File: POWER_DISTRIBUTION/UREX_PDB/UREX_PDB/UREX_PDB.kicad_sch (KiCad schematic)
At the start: 23 parts, among them IC1 TCAN1044VDDFR, IC5 TCA6408ARGTR, J12 S3B-PH-SM4-TB_LF__SN_, U1 ESP32-WROOM-32UE-R2

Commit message: fixed jarring pcb issues
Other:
- note added: "UARTS are flipped here issue:net is unused in actual board!"
- note removed: "UARTS are flipped here"
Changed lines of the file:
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@@
 		)
 	)
-	(text "UARTS are flipped here"
+	(text "UARTS are flipped here\nissue:net is unused in actual board!\n\n"
 		(exclude_from_sim no)
-		(at 113.792 71.628 0)
+		(at 121.92 71.12 0)
 		(effects
 			(font

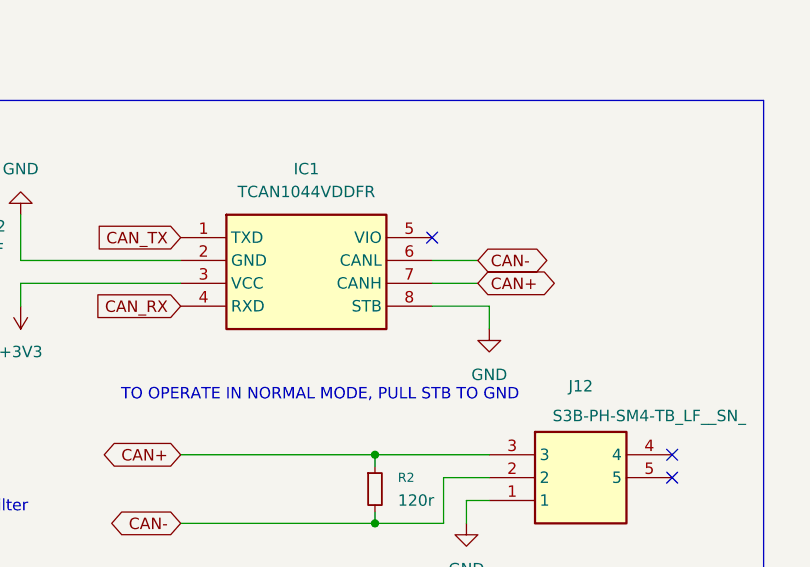
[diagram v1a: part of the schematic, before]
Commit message: changed CAN IC
TCAN1044 to TCAN332D, pin to pin compatible
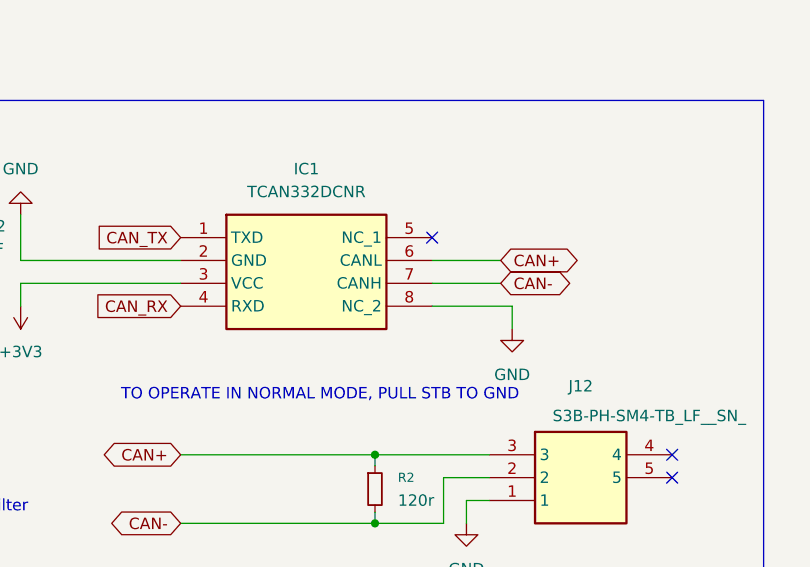
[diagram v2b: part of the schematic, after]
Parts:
- removed IC1: TCAN1044VDDFR, SamacSys_Parts:SOT65P280X110-8N, symbol SamacSys_COMMS:TCAN1044VDDFR
- added IC1: TCAN332DCNR, SOT65P280X145-8N, symbol SamacSys_Parts:TCAN332DCNR
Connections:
- net +3V3: now also IC1.3 (VCC)
- net CAN+: now also IC1.6 (CANL)
- net CAN-: now also IC1.7 (CANH)
- net CAN_RX: now also IC1.4 (RXD)
- net CAN_TX: now also IC1.1 (TXD)
- net GND: now also IC1.2 (GND), IC1.8 (NC_2)
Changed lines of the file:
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@@
 	(wire
 		(pts
-			(xy 33.02 44.45) (xy 44.45 44.45)
+			(xy 246.38 31.75) (xy 254 31.75)
 		)
 		(stroke
@@
 	(wire
 		(pts
-			(xy 240.03 60.96) (xy 247.65 60.96)
+			(xy 33.02 44.45) (xy 44.45 44.45)
 		)
 		(stroke
@@
 	(wire
 		(pts
-			(xy 252.73 36.83) (xy 252.73 39.37)
+			(xy 240.03 60.96) (xy 247.65 60.96)
 		)
 		(stroke
@@
 	(wire
 		(pts
-			(xy 246.38 31.75) (xy 251.46 31.75)
+			(xy 255.27 36.83) (xy 255.27 39.37)
 		)
 		(stroke
@@
 	(wire
 		(pts
-			(xy 246.38 36.83) (xy 252.73 36.83)
+			(xy 250.19 58.42) (xy 250.19 60.96)
 		)
 		(stroke
@@
 	(wire
 		(pts
-			(xy 250.19 58.42) (xy 250.19 60.96)
+			(xy 203.2 78.74) (xy 203.2 82.55)
 		)
 		(stroke
@@
 	(wire
 		(pts
-			(xy 203.2 78.74) (xy 203.2 82.55)
+			(xy 246.38 34.29) (xy 254 34.29)
 		)
 		(stroke
@@
 	(wire
 		(pts
-			(xy 246.38 34.29) (xy 251.46 34.29)
+			(xy 218.44 60.96) (xy 240.03 60.96)
 		)
 		(stroke
@@
 	(wire
 		(pts
-			(xy 218.44 60.96) (xy 240.03 60.96)
+			(xy 240.03 53.34) (xy 252.73 53.34)
 		)
 		(stroke
@@
 	(wire
 		(pts
-			(xy 240.03 53.34) (xy 252.73 53.34)
+			(xy 198.12 127) (xy 198.12 120.65)
 		)
 		(stroke
@@
 	(wire
 		(pts
-			(xy 198.12 127) (xy 198.12 120.65)
+			(xy 246.38 36.83) (xy 255.27 36.83)
 		)
 		(stroke
@@
 	(global_label "CAN-"
 		(shape bidirectional)
-		(at 251.46 31.75 0)
+		(at 254 34.29 0)
 		(fields_autoplaced yes)
 		(effects
@@
 		)
 		(property "Intersheetrefs" "${INTERSHEET_REFS}"
-			(at 260.818 31.75 0)
+			(at 263.358 34.29 0)
 			(hide yes)
 			(show_name no)
@@
 	(global_label "CAN+"
 		(shape bidirectional)
-		(at 251.46 34.29 0)
+		(at 254 31.75 0)
 		(fields_autoplaced yes)
 		(effects
@@
 		)
 		(property "Intersheetrefs" "${INTERSHEET_REFS}"
-			(at 260.818 34.29 0)
+			(at 263.358 31.75 0)
 			(hide yes)
 			(show_name no)
@@
 	)
 	(symbol
-		(lib_id "SamacSys_COMMS:TCAN1044VDDFR")
-		(at 218.44 29.21 0)
-		(unit 1)
-		(body_style 1)
-		(exclude_from_sim no)
-		(in_bom yes)
-		(on_board yes)
-		(in_pos_files yes)
-		(dnp no)
-		(fields_autoplaced yes)
-		(property "Reference" "IC1"
-			(at 232.41 21.59 0)
-			(show_name no)
-			(do_not_autoplace no)
-			(effects
-				(font
-					(size 1.27 1.27)
-				)
-			)
-		)
-		(property "Value" "TCAN1044VDDFR"
-			(at 232.41 24.13 0)
-			(show_name no)
-			(do_not_autoplace no)
-			(effects
-				(font
-					(size 1.27 1.27)
-				)
-			)
-		)
-		(property "Footprint" "SamacSys_Parts:SOT65P280X110-8N"
-			(at 242.57 124.13 0)
-			(hide yes)
-			(show_name no)
-			(do_not_autoplace no)
-			(effects
-				(font
-					(size 1.27 1.27)
-				)
-				(justify left top)
-			)
-		)
-		(property "Datasheet" "https://www.ti.com/lit/gpn/TCAN1044V"
-			(at 242.57 224.13 0)
-			(hide yes)
-			(show_name no)
-			(do_not_autoplace no)
-			(effects
-				(font
-					(size 1.27 1.27)
-				)
-				(justify left top)
-			)
-		)
-		(property "Description" "CAN XCVR WITH OPTIONAL FD"
-			(at 218.44 29.21 0)
-			(hide yes)
-			(show_name no)
-			(do_not_autoplace no)
-			(effects
-				(font
-					(size 1.27 1.27)
-				)
-			)
-		)
-		(property "Height" "1.1"
-			(at 242.57 424.13 0)
-			(hide yes)
-			(show_name no)
-			(do_not_autoplace no)
-			(effects
-				(font
-					(size 1.27 1.27)
-				)
-				(justify left top)
-			)
-		)
-		(property "Mouser Part Number" "595-TCAN1044VDDFR"
-			(at 242.57 524.13 0)
-			(hide yes)
-			(show_name no)
-			(do_not_autoplace no)
-			(effects
-				(font
-					(size 1.27 1.27)
-				)
-				(justify left top)
-			)
-		)
-		(property "Mouser Price/Stock" "https://www.mouser.co.uk/ProductDetail/Texas-Instruments/TCAN1044VDDFR?qs=xZ%2FP%252Ba9zWqaHsa9RvdIfqA%3D%3D"
-			(at 242.57 624.13 0)
-			(hide yes)
-			(show_name no)
-			(do_not_autoplace no)
-			(effects
-				(font
-					(size 1.27 1.27)
-				)
-				(justify left top)
-			)
-		)
-		(property "Manufacturer_Name" "Texas Instruments"
-			(at 242.57 724.13 0)
-			(hide yes)
-			(show_name no)
-			(do_not_autoplace no)
-			(effects
-				(font
-					(size 1.27 1.27)
-				)
-				(justify left top)
-			)
-		)
-		(property "Manufacturer_Part_Number" "TCAN1044VDDFR"
-			(at 242.57 824.13 0)
-			(hide yes)
-			(show_name no)
-			(do_not_autoplace no)
-			(effects
-				(font
-					(size 1.27 1.27)
-				)
-				(justify left top)
-			)
-		)
-		(pin "4"
-		)
-		(pin "8"
-		)
-		(pin "5"
-		)
-		(pin "2"
-		)
-		(pin "3"
-		)
-		(pin "1"
-		)
-		(pin "7"
-		)
-		(pin "6"
-		)
-		(instances
-			(project "UREX_PDB"
-				(path "/a38818e8-e869-45a4-b642-866064a1ec6a"
-					(reference "IC1")
-					(unit 1)
-				)
-			)
-		)
-	)
-	(symbol
 		(lib_id "Device:R_Small")
 		(at 21.59 149.86 180)
@@
 	(symbol
 		(lib_id "power:GND")
-		(at 252.73 39.37 0)
+		(at 255.27 39.37 0)
 		(unit 1)
 		(body_style 1)
@@
 		(fields_autoplaced yes)
 		(property "Reference" "#PWR0217"
-			(at 252.73 45.72 0)
+			(at 255.27 45.72 0)
 			(hide yes)
 			(show_name no)
@@
 		)
 		(property "Value" "GND"
-			(at 252.73 44.45 0)
+			(at 255.27 44.45 0)
 			(show_name no)
 			(do_not_autoplace no)
@@
 		)
 		(property "Footprint" ""
-			(at 252.73 39.37 0)
+			(at 255.27 39.37 0)
 			(hide yes)
 			(show_name no)
@@
 		)
 		(property "Datasheet" ""
-			(at 252.73 39.37 0)
+			(at 255.27 39.37 0)
 			(hide yes)
 			(show_name no)
@@
 		)
 		(property "Description" "Power symbol creates a global label with name \"GND\" , ground"
-			(at 252.73 39.37 0)
+			(at 255.27 39.37 0)
 			(hide yes)
 			(show_name no)
@@
 					(unit 1)
 				)
+			)
+		)
+	)
+	(symbol
+		(lib_id "SamacSys_Parts:TCAN332DCNR")
+		(at 218.44 29.21 0)
+		(unit 1)
+		(body_style 1)
+		(exclude_from_sim no)
+		(in_bom yes)
+		(on_board yes)
+		(in_pos_files yes)
+		(dnp no)
+		(fields_autoplaced yes)
+		(property "Reference" "IC1"
+			(at 232.41 21.59 0)
+			(show_name no)
+			(do_not_autoplace no)
+			(effects
+				(font
+					(size 1.27 1.27)
+				)
+			)
+		)
+		(property "Value" "TCAN332DCNR"
+			(at 232.41 24.13 0)
+			(show_name no)
+			(do_not_autoplace no)
+			(effects
+				(font
+					(size 1.27 1.27)
+				)
+			)
+		)
+		(property "Footprint" "SOT65P280X145-8N"
+			(at 242.57 124.13 0)
+			(hide yes)
+			(show_name no)
+			(do_not_autoplace no)
+			(effects
+				(font
+					(size 1.27 1.27)
+				)
+				(justify left top)
+			)
+		)
+		(property "Datasheet" "http://www.ti.com/lit/ds/symlink/tcan330.pdf"
+			(at 242.57 224.13 0)
+			(hide yes)
+			(show_name no)
+			(do_not_autoplace no)
+			(effects
+				(font
+					(size 1.27 1.27)
+				)
+				(justify left top)
+			)
+		)
+		(property "Description" "CAN Interface IC 3.3-V CAN Transceivers 8-SOT-23 -40 to 125"
+			(at 218.44 29.21 0)
+			(hide yes)
+			(show_name no)
+			(do_not_autoplace no)
+			(effects
+				(font
+					(size 1.27 1.27)
+				)
+			)
+		)
+		(property "Height" "1.45"
+			(at 242.57 424.13 0)
+			(hide yes)
+			(show_name no)
+			(do_not_autoplace no)
+			(effects
+				(font
+					(size 1.27 1.27)
+				)
+				(justify left top)
+			)
+		)
+		(property "Mouser Part Number" "595-TCAN332DCNR"
+			(at 242.57 524.13 0)
+			(hide yes)
+			(show_name no)
+			(do_not_autoplace no)
+			(effects
+				(font
+					(size 1.27 1.27)
+				)
+				(justify left top)
+			)
+		)
+		(property "Mouser Price/Stock" "https://www.mouser.co.uk/ProductDetail/Texas-Instruments/TCAN332DCNR?qs=n%252BTO0c4TDSae%2FgCyWFBOKw%3D%3D"
+			(at 242.57 624.13 0)
+			(hide yes)
+			(show_name no)
+			(do_not_autoplace no)
+			(effects
+				(font
+					(size 1.27 1.27)
+				)
+				(justify left top)
+			)
+		)
+		(property "Manufacturer_Name" "Texas Instruments"
+			(at 242.57 724.13 0)
+			(hide yes)
+			(show_name no)
+			(do_not_autoplace no)
+			(effects
+				(font
+					(size 1.27 1.27)
+				)
+				(justify left top)
+			)
+		)
+		(property "Manufacturer_Part_Number" "TCAN332DCNR"
+			(at 242.57 824.13 0)
+			(hide yes)
+			(show_name no)
+			(do_not_autoplace no)
+			(effects
+				(font
+					(size 1.27 1.27)
+				)
+				(justify left top)
+			)
+		)
+		(pin "7"
+		)
+		(pin "1"
+		)
+		(pin "6"
+		)
+		(pin "2"
+		)
+		(pin "3"
+		)
+		(pin "4"
+		)
+		(pin "8"
+		)
+		(pin "5"
+		)
+		(instances
+			(project "UREX_PDB"
+				(path "/a38818e8-e869-45a4-b642-866064a1ec6a"
+					(reference "IC1")
+					(unit 1)
+				)
